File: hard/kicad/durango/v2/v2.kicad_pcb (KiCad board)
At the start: 2 copper layers, 177.8 x 130.8 mm, 155 parts, among them J1 NANOLINK, J10 STEP, J11 EXPANSION, J2 AUDIO IN, J3 IOx, J4 LED, J605 COMPONENT VIDEO, J7 POWER IN, J706 COMPOSITE, J8 DEBUG, J9 CARTRIDGE, J905 SCART, Q1 BC548, Q2 BC548, Q3 BC548, Q307 BC548, Q4 BC548, Q5 BC548, Q608 BC548, Q609 BC548, Q610 BC548, Q611 BC548, Q906 BC548, SW1 RESET, SW2 NMI, U1 65C02, U10 74HC139, U104 74HC257, U105 74HC257, U11 74HC688, U12 74HC74, U124 74HC574, U125 74HC157, U126 74HC86, U127 74HC245, U13 74HC32, U14 74HC4040, U15 74HC4040, U16 74HC02, U17 74HC21, U18 74HC85, U19 CD4040, U20 74HC85, U204 74HC257, U205 74HC257, U22 74HC175, U224 74HC166, U227 74HC20, U23 74HC86, U29 74HC139, U3 62256, U31 74HC245, U32 74HC245, U321 74HC157, U428 74HC174, U530 74HC367, U6 74HC157, U7 74HC157, U8 74HC30, U9 74HC00, X1 28 MHz

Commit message: mostly clean v2 PCB
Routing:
- net GND: track 1762.0 -> 0.00 mm, vias 6 -> 0
- net +5V: track 1134.5 -> 0.00 mm, vias 19 -> 0
- net A2: track 595.3 -> 0.00 mm, vias 17 -> 0
- net D0: track 279.7 -> 0.00 mm, vias 8 -> 0
- net D3: track 262.5 -> 0.00 mm, vias 7 -> 0
- net D5: track 260.2 -> 0.00 mm, vias 7 -> 0
- net A14: track 257.2 -> 0.00 mm, vias 9 -> 0
- net D7: track 256.7 -> 0.00 mm, vias 6 -> 0
- net D1: track 253.7 -> 0.00 mm, vias 5 -> 0
- net D4: track 253.6 -> 0.00 mm, vias 9 -> 0
- net D2: track 248.3 -> 0.00 mm, vias 4 -> 0
- net D6: track 248.3 -> 0.00 mm, vias 6 -> 0
- net VA0: track 234.0 -> 0.00 mm, vias 3 -> 0
- net INVERT: track 229.1 -> 0.00 mm, vias 5 -> 0
- net A9: track 227.8 -> 0.00 mm, vias 7 -> 0
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
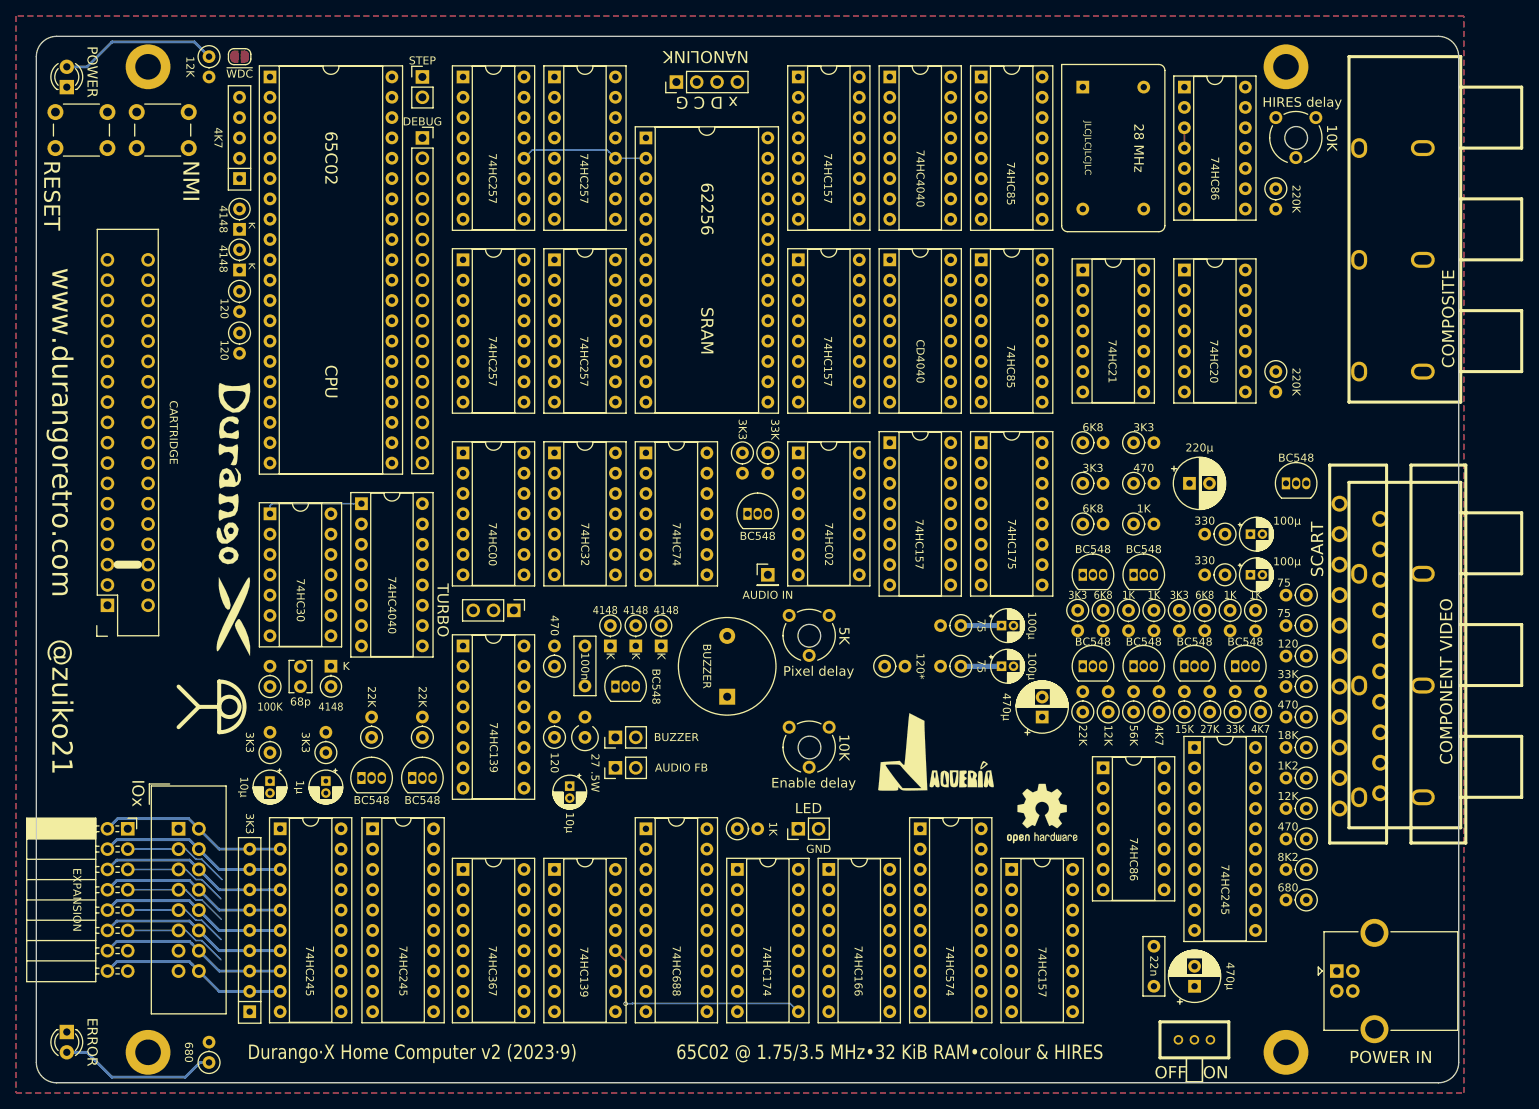
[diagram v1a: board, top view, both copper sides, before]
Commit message: all power pads done
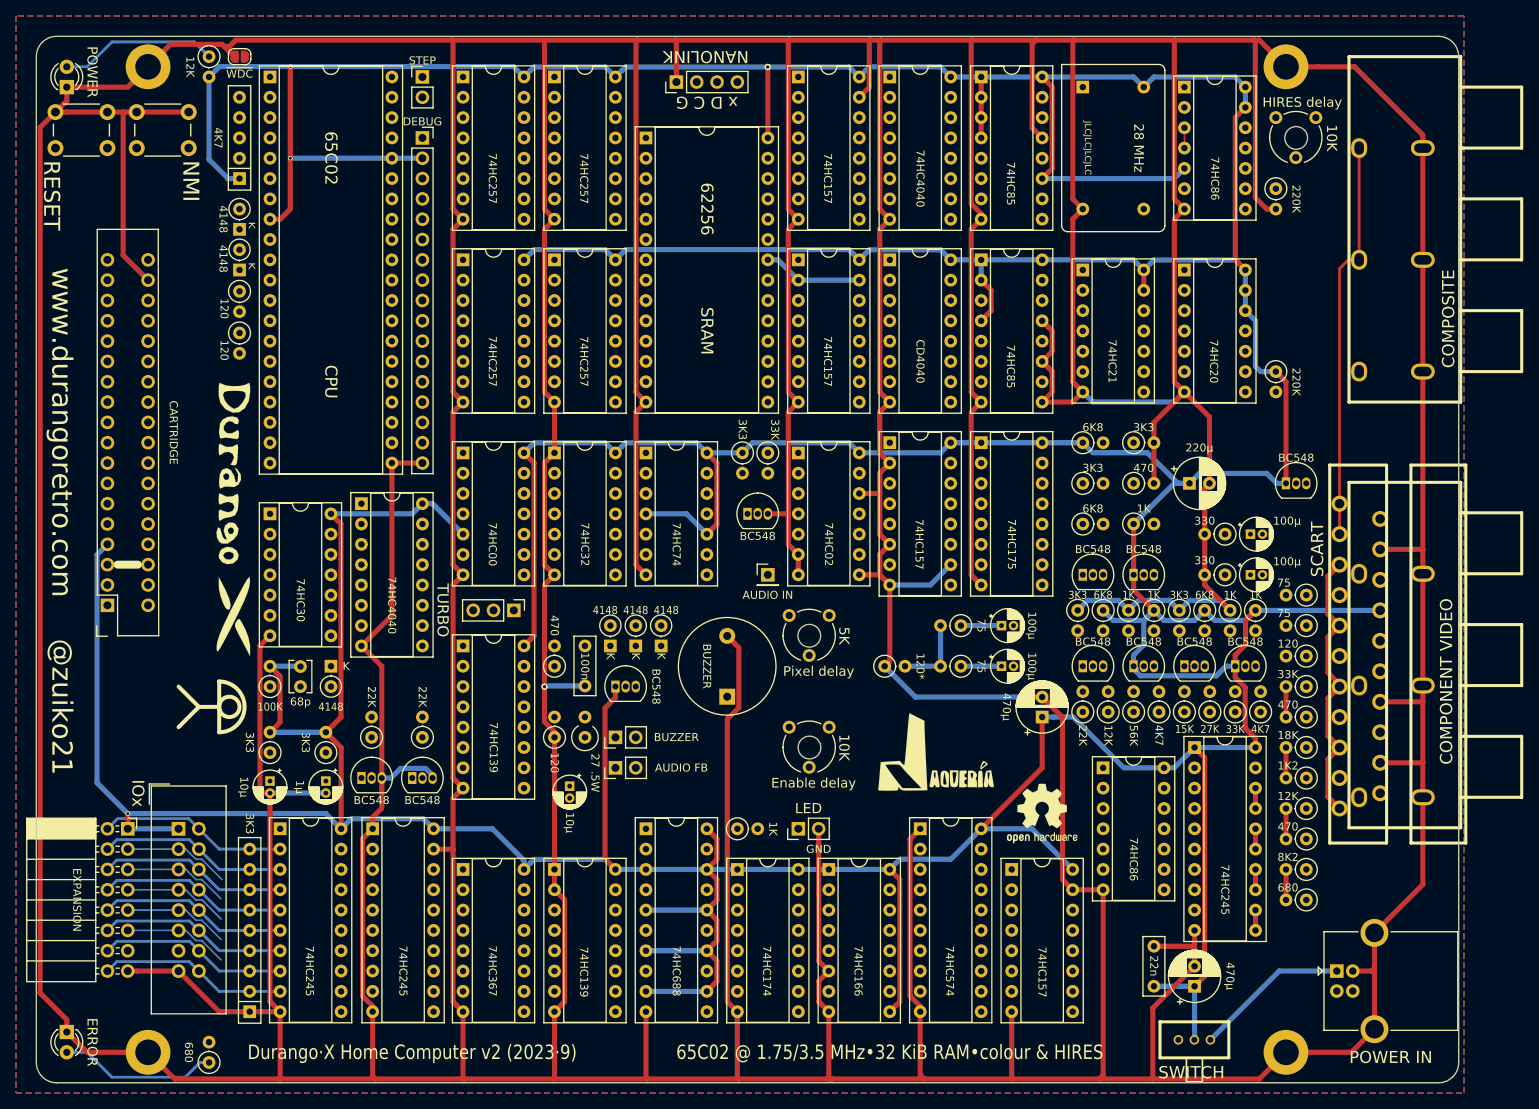
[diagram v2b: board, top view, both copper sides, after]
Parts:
- JP3: value OFF ON -> SWITCH
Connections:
- J9 pad 21: A2 -> A10
- J9 pad 24: A2 -> A1
- U1 pad 10: A2 -> A1
- U1 pad 19: A2 -> A10
- U105 pad 13: A2 -> A1
- U11 pad 8: A2 -> A10
- U205 pad 13: A2 -> A1
- U32 pad 17: A2 -> A1
- U6 pad 13: A2 -> A10
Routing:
- net GND: track 0.00 -> 1930.4 mm, vias 0 -> 1
- net +5V: track 0.00 -> 1075.6 mm, vias 0 -> 4
- net AUDIO: track 0.00 -> 50.1 mm
- net /Video & Clock generation/~FLAGS: track 29.3 -> 0.00 mm, vias 1 -> 0
- net /Power and Extras/+5V_IN: track 0.00 -> 19.4 mm
- net /MA1: track 16.1 -> 0.00 mm
- net /CNT2K: track 12.5 -> 0.00 mm
- net MIX: track 0.00 -> 9.53 mm
- net DRED: track 0.00 -> 6.35 mm
- net DGLO: track 0.00 -> 6.35 mm
- net DGHI: track 0.00 -> 6.35 mm
- net DBLU: track 0.00 -> 6.35 mm

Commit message: most AV analog signals
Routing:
- net /Video & Clock generation/HPIX: track 0.00 -> 142.9 mm, vias 0 -> 1
- net AUDIO: track 50.1 -> 184.9 mm, vias 0 -> 2
- net SCLK: track 0.00 -> 126.7 mm, vias 0 -> 2
- net /Video & Clock generation/VIN: track 0.00 -> 85.7 mm, vias 0 -> 1
- net AUDIO_IN: track 0.00 -> 84.1 mm, vias 0 -> 1
- net /Power and Extras/Y: track 0.00 -> 70.0 mm, vias 0 -> 1
- net LUMA: track 0.00 -> 56.6 mm
- net /Video & Clock generation/~DCDE: track 0.00 -> 56.4 mm
- net /Video & Clock generation/RGB: track 0.00 -> 54.6 mm, vias 0 -> 1
- net DGHI: track 6.35 -> 50.5 mm, vias 0 -> 1
- net VCLK: track 0.00 -> 43.5 mm
- net DGLO: track 6.35 -> 46.1 mm
- net /Video & Clock generation/~HVG: track 0.00 -> 39.6 mm, vias 0 -> 1
- net /Video & Clock generation/DHVD: track 0.00 -> 36.8 mm
- net /Video & Clock generation/XGL: track 0.00 -> 36.1 mm, vias 0 -> 1
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
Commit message: many address lines
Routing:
- net A1: track 0.00 -> 142.4 mm, vias 0 -> 2
- net A3: track 0.00 -> 137.9 mm, vias 0 -> 2
- net D5: track 0.00 -> 132.0 mm, vias 0 -> 2
- net A0: track 0.00 -> 130.9 mm, vias 0 -> 2
- net A2: track 0.00 -> 129.4 mm, vias 0 -> 2
- net A11: track 0.00 -> 113.5 mm, vias 0 -> 1
- net A14: track 0.00 -> 100.3 mm, vias 0 -> 1
- net A10: track 0.00 -> 87.7 mm, vias 0 -> 1
- net A12: track 0.00 -> 86.7 mm, vias 0 -> 1
- net A13: track 0.00 -> 85.2 mm, vias 0 -> 1
- net A9: track 0.00 -> 76.1 mm, vias 0 -> 1
- net A8: track 0.00 -> 74.7 mm
- net D1: track 0.00 -> 59.5 mm, vias 0 -> 1
- net D0: track 8.67 -> 67.1 mm, vias 0 -> 1
- net /PHI2: track 0.00 -> 58.4 mm
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
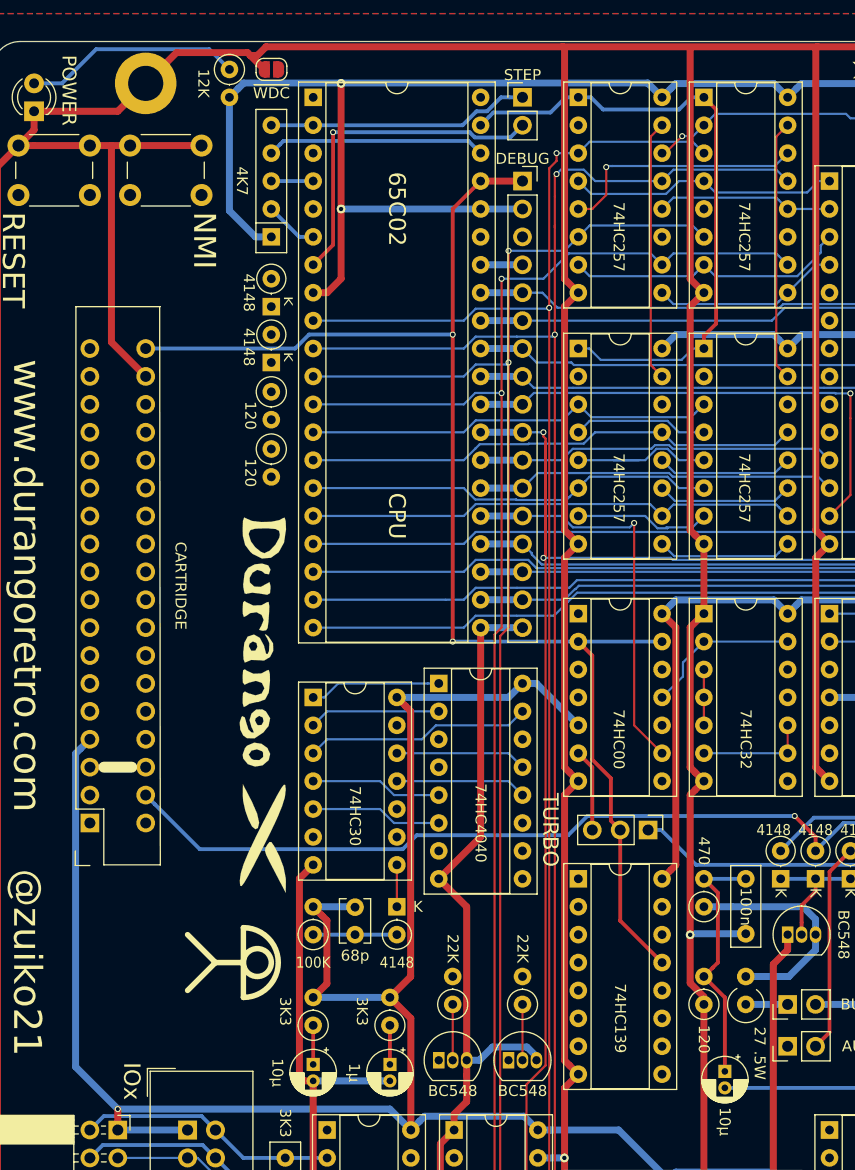
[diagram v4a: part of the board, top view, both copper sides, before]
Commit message: connect most cartridge pins
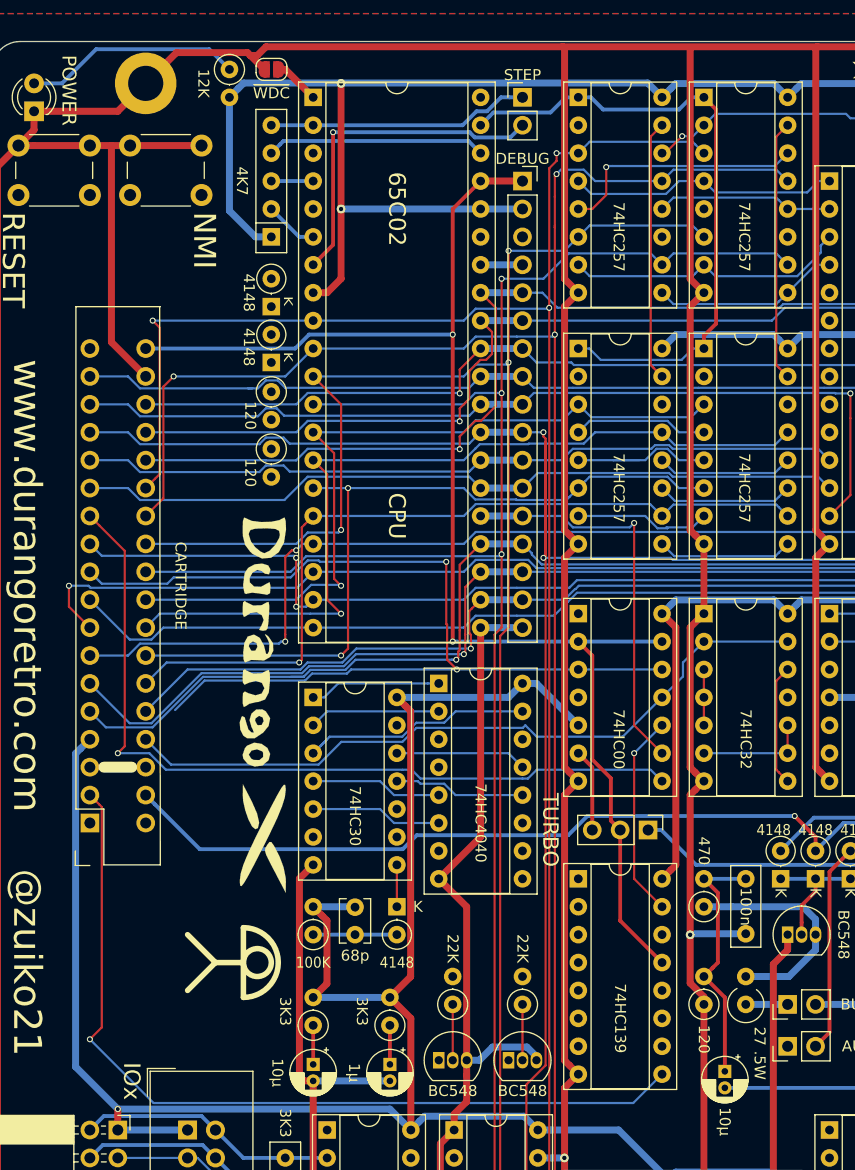
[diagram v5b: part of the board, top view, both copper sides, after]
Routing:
- net ~ROM_OE: track 0.00 -> 89.9 mm, vias 0 -> 2
- net ~IOC: track 0.00 -> 78.7 mm, vias 0 -> 1
- net ~ROM_CS: track 0.00 -> 74.4 mm, vias 0 -> 1
- net ~WE: track 14.3 -> 65.6 mm
- net A14: track 100.3 -> 149.5 mm, vias 1 -> 2
- net A13: track 85.2 -> 131.5 mm, vias 1 -> 2
- net D0: track 67.1 -> 112.6 mm, vias 1 -> 2
- net D1: track 59.5 -> 99.7 mm, vias 1 -> 2
- net D3: track 56.7 -> 94.1 mm
- net D7: track 32.9 -> 70.2 mm
- net D4: track 46.0 -> 83.1 mm
- net D5: track 132.0 -> 168.9 mm
- net D6: track 32.9 -> 69.8 mm
- net A12: track 86.7 -> 123.6 mm, vias 1 -> 2
- net D2: track 57.3 -> 91.2 mm, vias 1 -> 2
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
